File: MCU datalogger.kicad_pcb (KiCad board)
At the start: 4 copper layers, 51 x 32.8 mm, 29 parts, among them J1 Conn_01x04_Pin, J2 Conn_01x04_Pin, J3 Conn_01x09_Pin, J4 Conn_02x03_Odd_Even, U1 24LC1025, U2 24LC1025, U3 ATMEGA328P-AU, U4 DS1337S_, Y1 32.768KHz, Y2 16MHz

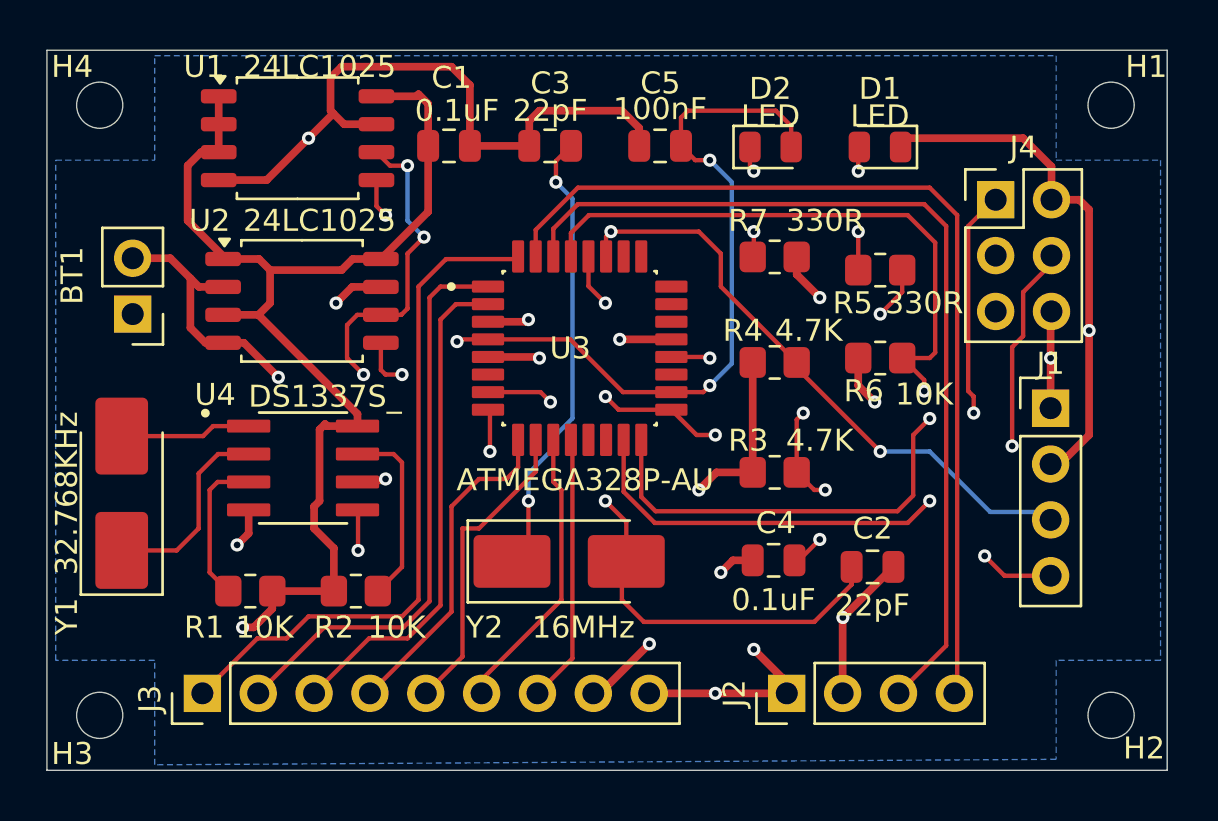
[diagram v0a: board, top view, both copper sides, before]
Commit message: Add copper layer
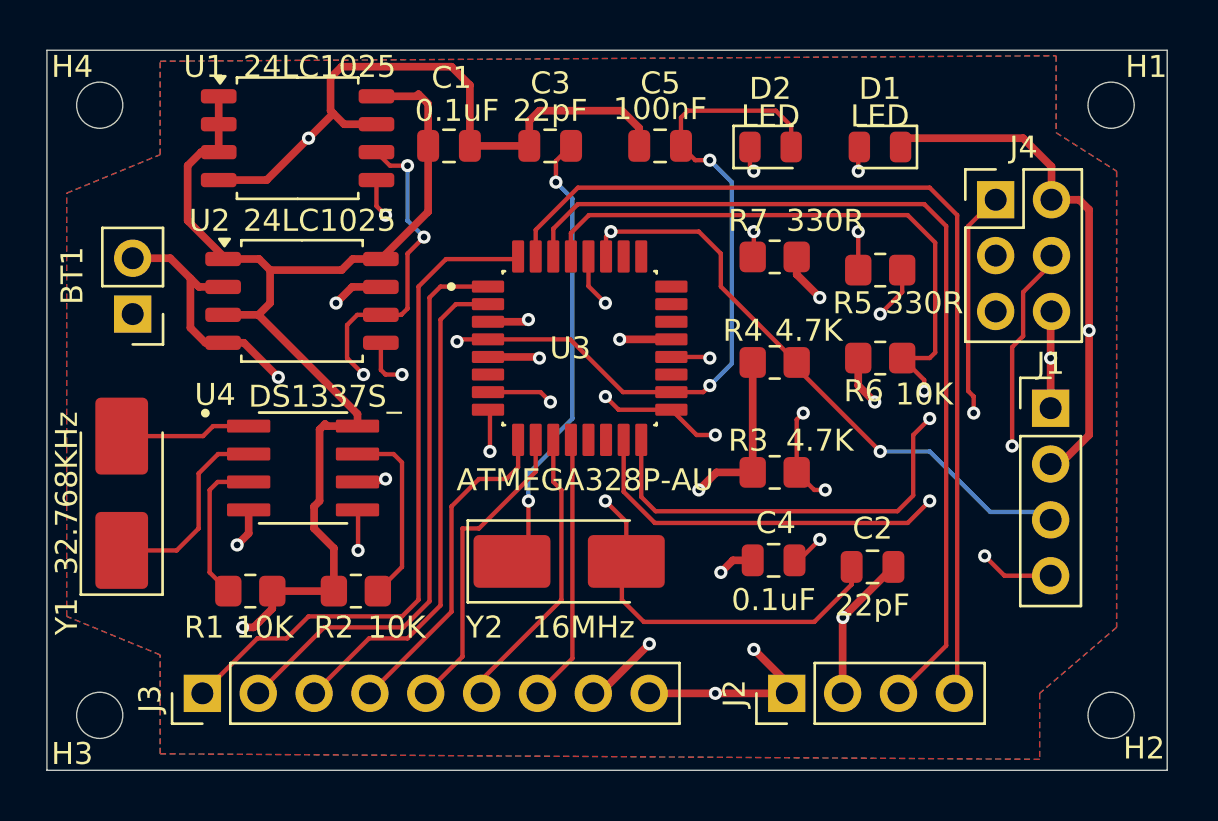
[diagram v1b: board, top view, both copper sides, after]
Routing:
- added copper zone on F.Cu, net GND
- removed copper zone on In2.Cu, net /VCC
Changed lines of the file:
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@@
 		(net 2)
 		(net_name "GND")
-		(layer "B.Cu")
+		(layers "F.Cu" "B.Cu")
 		(hatch edge 0.5)
-		(connect_pads
-			(clearance 0.5)
-		)
-		(min_thickness 0.25)
-		(filled_areas_thickness no)
-		(fill yes
-			(mode hatch)
-			(thermal_gap 0.5)
-			(thermal_bridge_width 0.5)
-			(hatch_thickness 1)
-			(hatch_gap 1.5)
-			(hatch_orientation 0)
-			(hatch_border_algorithm hatch_thickness)
-			(hatch_min_hole_area 0.3)
-		)
-		(polygon
-			(pts
-				(xy 1941.75 2090) (xy 1946.25 2090) (xy 1946.25 2085.25) (xy 1987.25 2085.25) (xy 1987.25 2090)
-				(xy 1992 2090) (xy 1992 2112.75) (xy 1987.25 2112.75) (xy 1987.25 2117.25) (xy 1946.25 2117.5) (xy 1946.25 2112.75)
-				(xy 1941.75 2112.75)
-			)
-		)
-	)
-	(zone
-		(net 3)
-		(net_name "/VCC")
-		(layer "In2.Cu")
-		(hatch edge 0.5)
-		(priority 1)
 		(connect_pads
 			(clearance 0.5)
@@
 		(polygon
 			(pts
-				(xy 1987.25 2085.25) (xy 1987.25 2090) (xy 1992 2090) (xy 1992 2112.75) (xy 1987.25 2112.75) (xy 1987.25 2117.25)
-				(xy 1946.25 2117.5) (xy 1946.25 2112.75) (xy 1941.75 2112.75) (xy 1941.75 2090) (xy 1946.25 2090)
-				(xy 1946.25 2085.25)
+				(xy 1987.25 2085.25) (xy 1987.25 2088.75) (xy 1990 2090.5) (xy 1990 2111.25) (xy 1986.5 2114.25)
+				(xy 1986.5 2117.25) (xy 1946.5 2117) (xy 1946.5 2112.5) (xy 1942.25 2110.75) (xy 1942.25 2091.5)
+				(xy 1946.5 2089.75) (xy 1946.5 2085.5)
 			)
 		)
